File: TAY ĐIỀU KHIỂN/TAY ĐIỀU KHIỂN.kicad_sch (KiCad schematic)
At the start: 8 parts, among them U1 ESP32-WROOM-32, U2 NRF24L01_Breakout

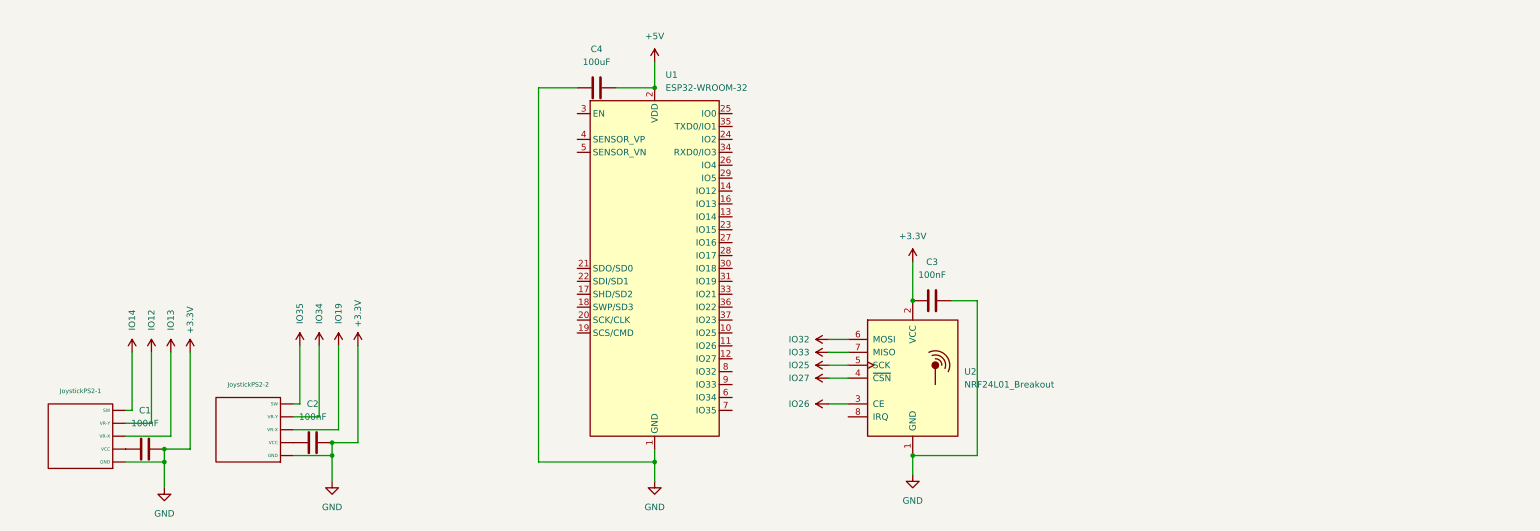
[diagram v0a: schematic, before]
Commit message: ve lai schematic cua tay cam, PCB DNHK da ve on
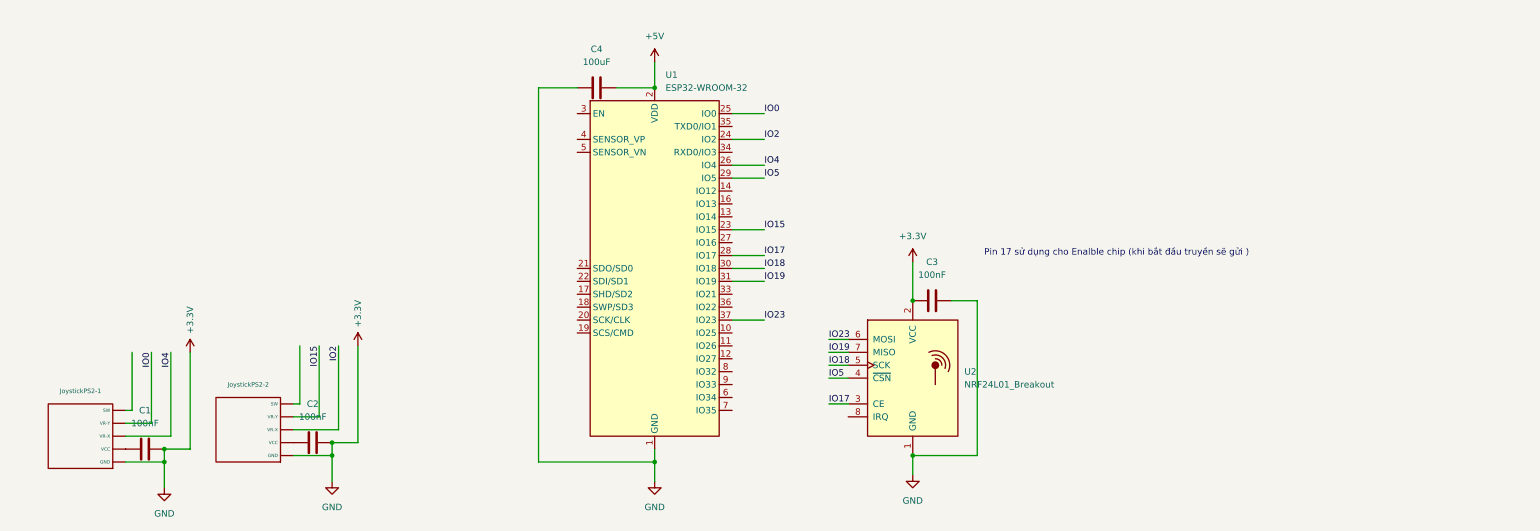
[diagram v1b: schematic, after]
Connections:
- net IO12 is gone; now on net IO4: JoystickPS2-1. (SW)
- net IO13 is gone; now on net IO4: JoystickPS2-1. (SW)
- net IO14 is gone; now on net IO4: JoystickPS2-1. (SW)
- net IO25 is gone; now on net IO18: U2.5 (SCK)
- net IO26 is gone; now on net IO17: U2.3 (CE)
- net IO27 is gone; now on net IO5: U2.4 (~{CSN})
- net IO32 is gone; now on net IO23: U2.6 (MOSI)
- net IO33 is gone; now on net IO19: U2.7 (MISO)
- net IO34 is gone; now on net IO2: JoystickPS2-2. (SW)
- net IO35 is gone; now on net IO2: JoystickPS2-2. (SW)
- net IO19: now also U1.31 (IO19); no longer JoystickPS2-2. (SW)
- net IO15: now reaches U1.23 (IO15)
- net IO15: now also JoystickPS2-2. (SW)
- net IO2: now reaches U1.24 (IO2)
- net IO0: now reaches U1.25 (IO0)
- net IO0: now also JoystickPS2-1. (SW)
- net IO4: now reaches U1.26 (IO4)
- net IO17: now reaches U1.28 (IO17)
- net IO5: now reaches U1.29 (IO5)
- net IO18: now reaches U1.30 (IO18)
- net IO23: now reaches U1.37 (IO23)
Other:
- note added: "Pin 17 sử dụng cho Enalble chip (khi bắt đầu truyền sẽ gửi )"

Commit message: Add ESP library and comments on Duy Khang's schem
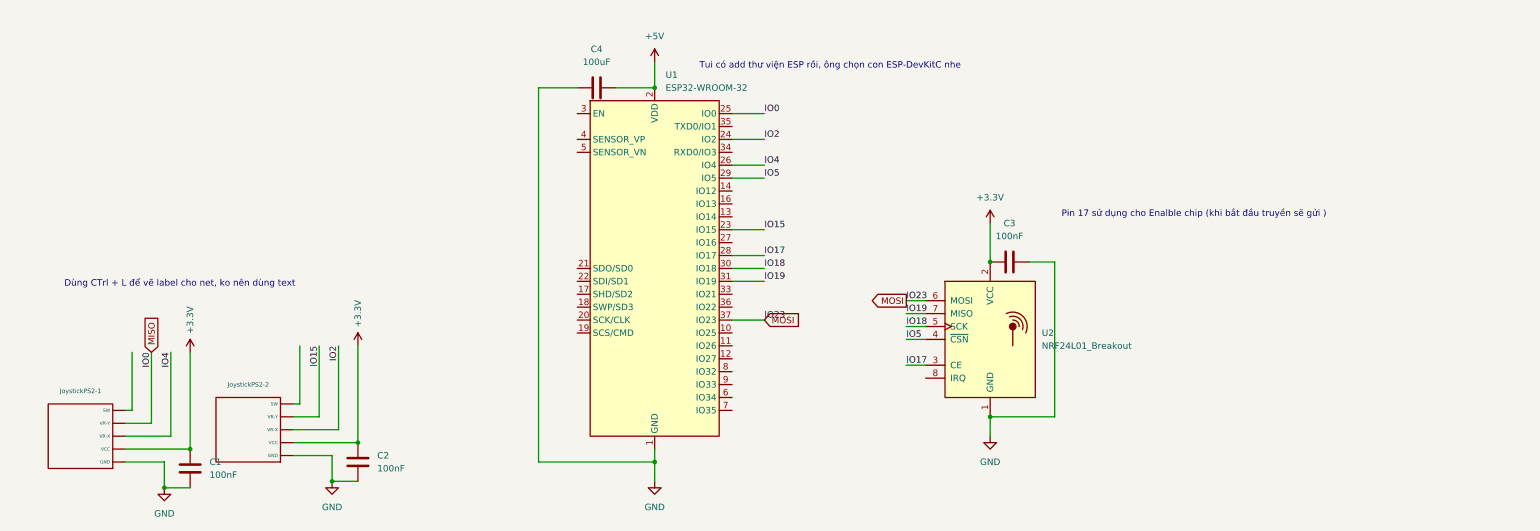
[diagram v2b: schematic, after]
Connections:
- net IO0 is gone; now on net MISO: JoystickPS2-1. (SW), U1.25 (IO0)
- net +3.3V: now also C1.1; no longer C1.2, C3.2, C4.1, U1.1 (GND), U1.15 (GND), U1.38 (GND), U1.39 (GND), U2.1 (GND)
- net MISO: now reaches JoystickPS2-1. (SW)
- net GND: now reaches C2.1, JoystickPS2-2. (SW)
- net GND: now also C1.2, C3.2, C4.1, JoystickPS2-1. (SW), U1.1 (GND), U1.15 (GND), U1.38 (GND), U1.39 (GND), U2.1 (GND)
- net IO23 renamed MOSI
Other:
- note added: "Dùng CTrl + L để vẽ label cho net, ko nên dùng text"
- note added: "Tui có add thư viện ESP rồi, ông chọn con ESP-DevKitC nhe"
- moved on the sheet: C1, C3, U2

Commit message: NEW
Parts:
- removed U1: ESP32-WROOM-32, Connector_PinHeader_2.54mm:PinHeader_2x19_P2.54mm_Vertical, symbol RF_Module:ESP32-WROOM-32
- added U1: ESP32-DevKitC, PCM_Espressif:ESP32-DevKitC, symbol PCM_Espressif:ESP32-DevKitC
- C4: footprint Capacitor_THT:C_Disc_D5.0mm_W2.5mm_P2.50mm -> (none)
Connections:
- net IO15 is gone; now on net GPIO 21: JoystickPS2-2. (SW)
- net IO19 is gone; now on net MISO: U2.7 (MISO)
- net IO2 is gone; now on net GPIO 21: JoystickPS2-2. (SW)
- net IO4 is gone; now on net GPIO 4: JoystickPS2-1. (SW)
- net GND: now also U1.14 (GND), U1.32 (GND), U1.38 (GND)
- net MISO: now also U1.31 (GPIO19); no longer JoystickPS2-1. (SW)
- net MOSI: now also U1.37 (GPIO23)
- net GPIO 4: now reaches JoystickPS2-1. (SW)
- net GPIO 21: now reaches JoystickPS2-2. (SW)
- net +5V renamed +3V3
- net +3V3: now also U1.19 (5V)
- net IO17 renamed CE
- net CE: now also U1.28 (GPIO17)
- net IO18 renamed SCK
- net SCK: now also U1.30 (GPIO18)
- net IO5 renamed CSN
- net CSN: now also U1.29 (GPIO5)
- new net GPIO 0: JoystickPS2-2. (SW)
- new net GPIO 22: JoystickPS2-1. (SW)
- new net SW1: U1.36 (GPIO22)
- new net SW2: U1.33 (GPIO21)
- new net VR - X1: U1.26 (ADC2_CH0/GPIO4)
- new net VR - Y2: U1.25 (GPIO0/BOOT/ADC2_CH1)
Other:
- note removed: "Tui có add thư viện ESP rồi, ông chọn con ESP-DevKitC nhe"
- moved on the sheet: C3, U2
